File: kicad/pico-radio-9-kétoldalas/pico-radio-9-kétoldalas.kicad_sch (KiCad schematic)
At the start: 54 parts, among them J1 FM antenna, J2 SW antenna, J3 MW/SW antenna kapcsoló, J4 HF Amplifier, J5 Batterry, Q1 PN2222A, Q2 PN2222A, Q3 PN2222A, SW1 Reset, U1 SI4732-A10-GS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

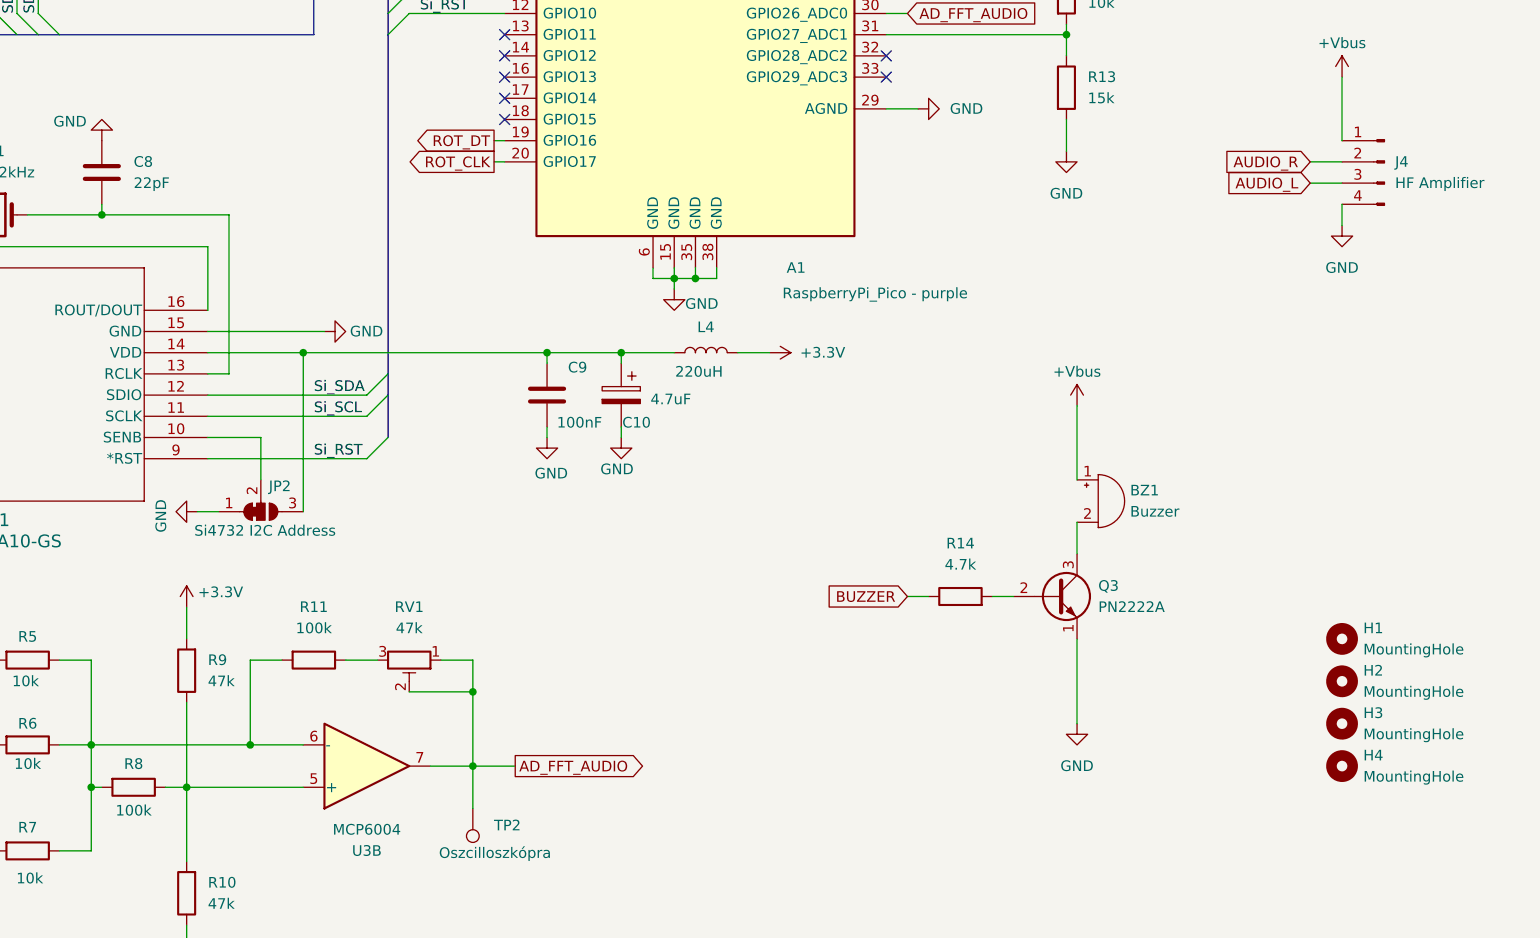
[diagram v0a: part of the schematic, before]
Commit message: Dual side PCB
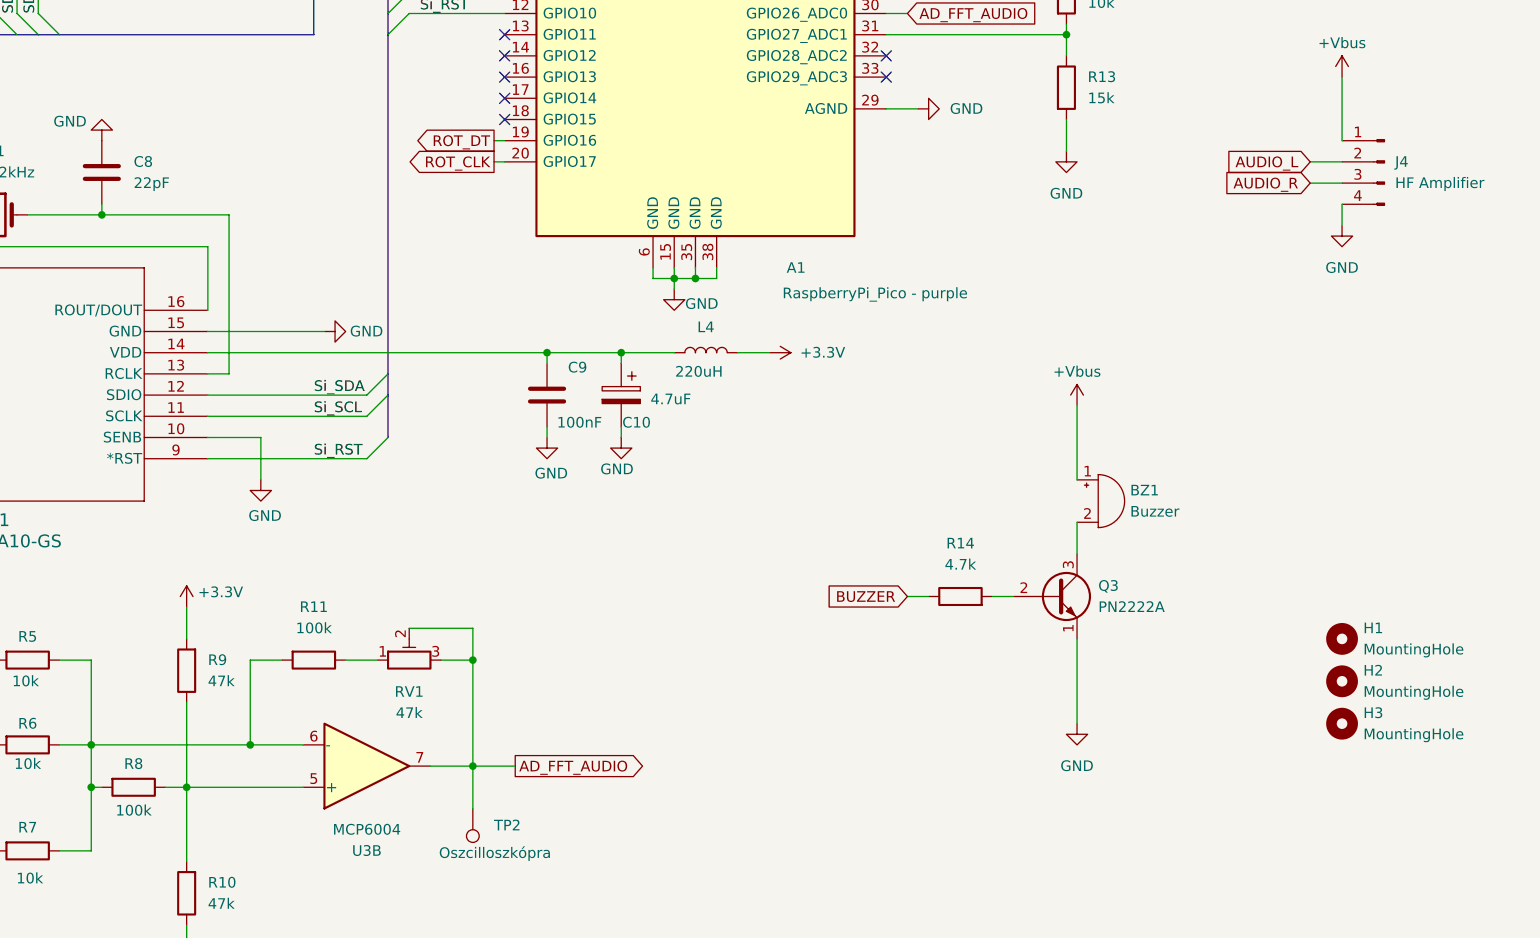
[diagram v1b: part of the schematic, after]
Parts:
- removed H4: MountingHole, MountingHole:MountingHole_3.2mm_M3, symbol Mechanical:MountingHole
- removed JP2: Si4732 I2C Address, Jumper:SolderJumper-3_P1.3mm_Bridged12_RoundedPad1.0x1.5mm, symbol Jumper:SolderJumper_3_Bridged12
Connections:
- net AD_FFT_AUDIO: now also RV1.3; no longer RV1.1
- net AUDIO_L: now also J4.2 (Pin_2); no longer J4.3 (Pin_3)
- net AUDIO_R: now also J4.3 (Pin_3); no longer J4.2 (Pin_2)
- net GND: now also U1.10 (SENB)
- net at R11.1: now also RV1.1; no longer RV1.3
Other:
- moved on the sheet: RV1

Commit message: Dual sided  PCB update
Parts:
- removed U4: KY-040, Rotary_Encoder:KY-040-PORT, symbol Device:KY-040
- added H4: MountingHole, MountingHole:MountingHole_3.2mm_M3, symbol Mechanical:MountingHole
- added J6: KY-040 Rotary, Connector_PinHeader_2.54mm:PinHeader_1x05_P2.54mm_Vertical, symbol Connector:Conn_01x05_Pin
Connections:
- net +3.3V: now also J6.4 (Pin_4)
- net GND: now also J6.5 (Pin_5)
- net ROT_CLK: now also J6.1 (Pin_1)
- net ROT_DT: now also J6.2 (Pin_2)
- net ROT_SW: now also J6.3 (Pin_3)
